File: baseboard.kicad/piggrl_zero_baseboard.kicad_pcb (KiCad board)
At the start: 2 copper layers, 101 x 43.9 mm, 62 parts, among them P1 PowerBoost 500c, P2 I2C, P3 USB_A, P4 Serial, Q1 IRF7309IPBF, Q3 Q_PMOS_GSD, Q4 MMBT2222, SW1 SW_PUSH, U1 gpio-header_zero, U2 2.2_tft_ili9340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

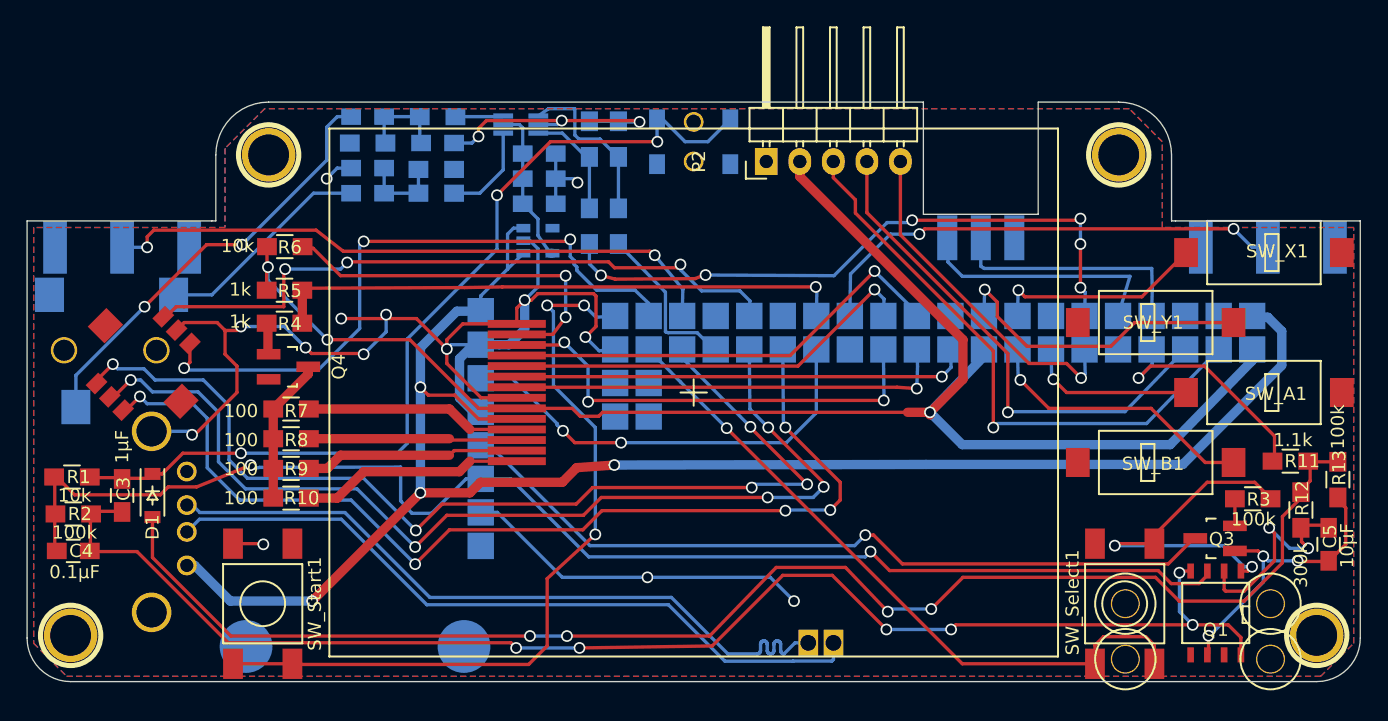
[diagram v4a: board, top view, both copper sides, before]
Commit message: ditch mosfet as softpower inverter and use same BJT transistor as the one used for the backlight
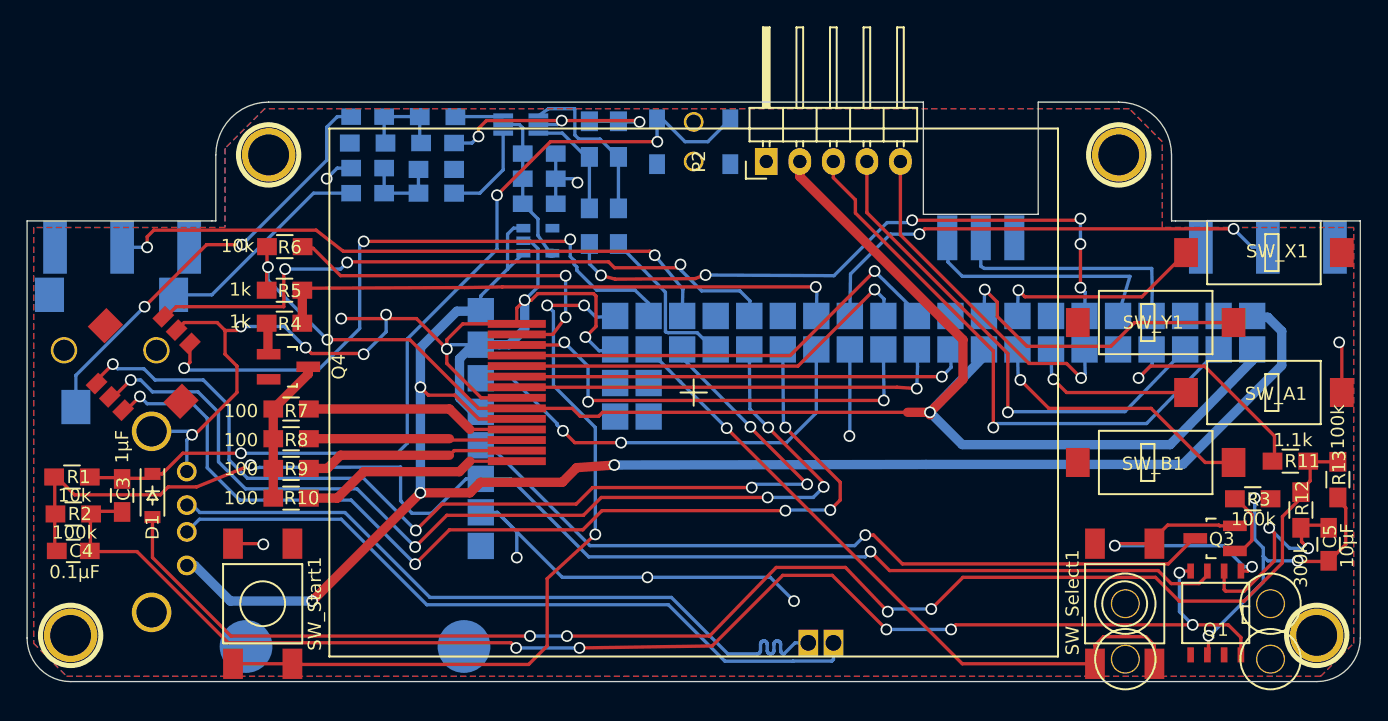
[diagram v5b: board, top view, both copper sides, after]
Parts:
- Q3: value Q_PMOS_GSD -> MMBT2222
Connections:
- Q3 pad 1: /soft_power_button/Vout -> Net-(Q3-Pad1)
- Q3 pad 2: Net-(Q3-Pad2) -> GND
- R3 pad 1: Net-(Q3-Pad2) -> Net-(Q3-Pad1)
- R3 pad 2: GND -> /soft_power_button/Vout
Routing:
- net GND: track 174.9 -> 187.4 mm, vias 19 -> 22
- net Net-(Q3-Pad1): track 0.00 -> 5.36 mm
- net /soft_power_button/Vout: track 22.2 -> 25.9 mm
- net Net-(Q3-Pad2): track 2.05 -> 0.00 mm

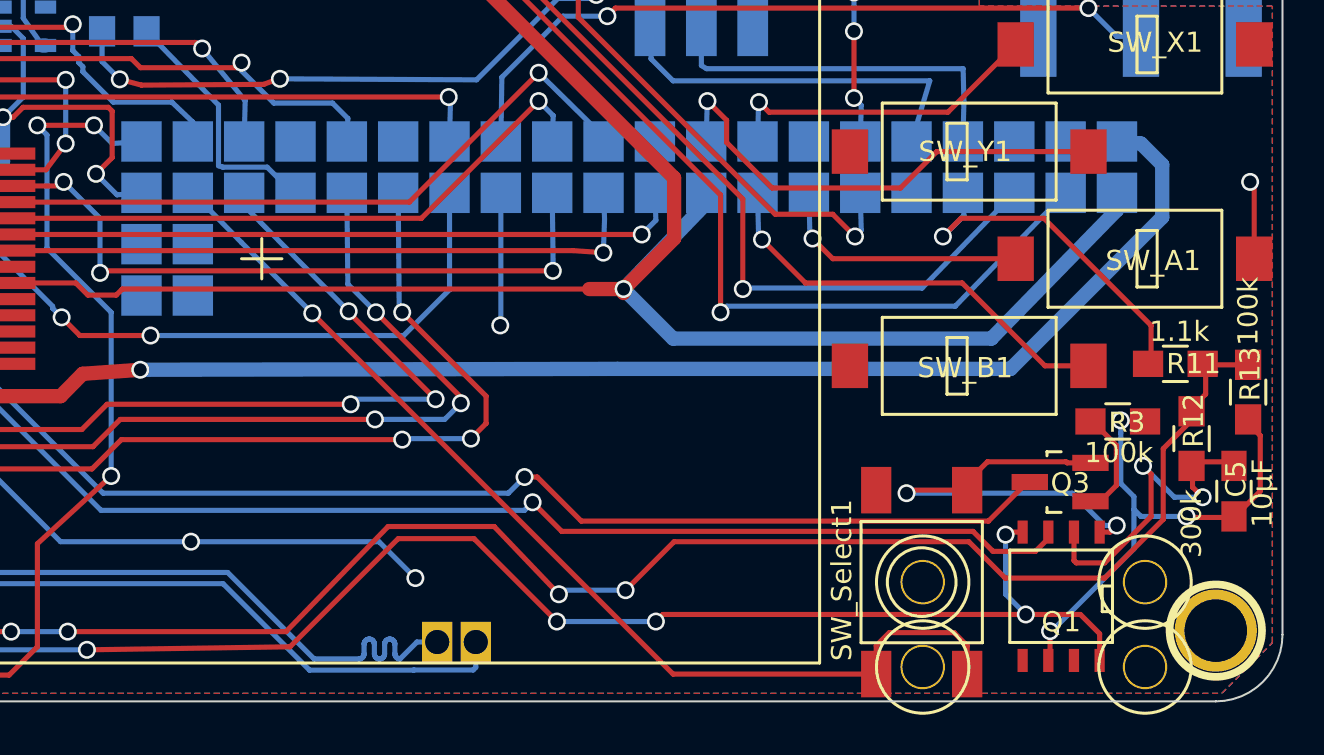
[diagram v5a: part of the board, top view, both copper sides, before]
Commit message: turns out we don't need the transistor (Q3) at all... so remove it, leaving only the 100k pulldown on the powerboosts enable pin
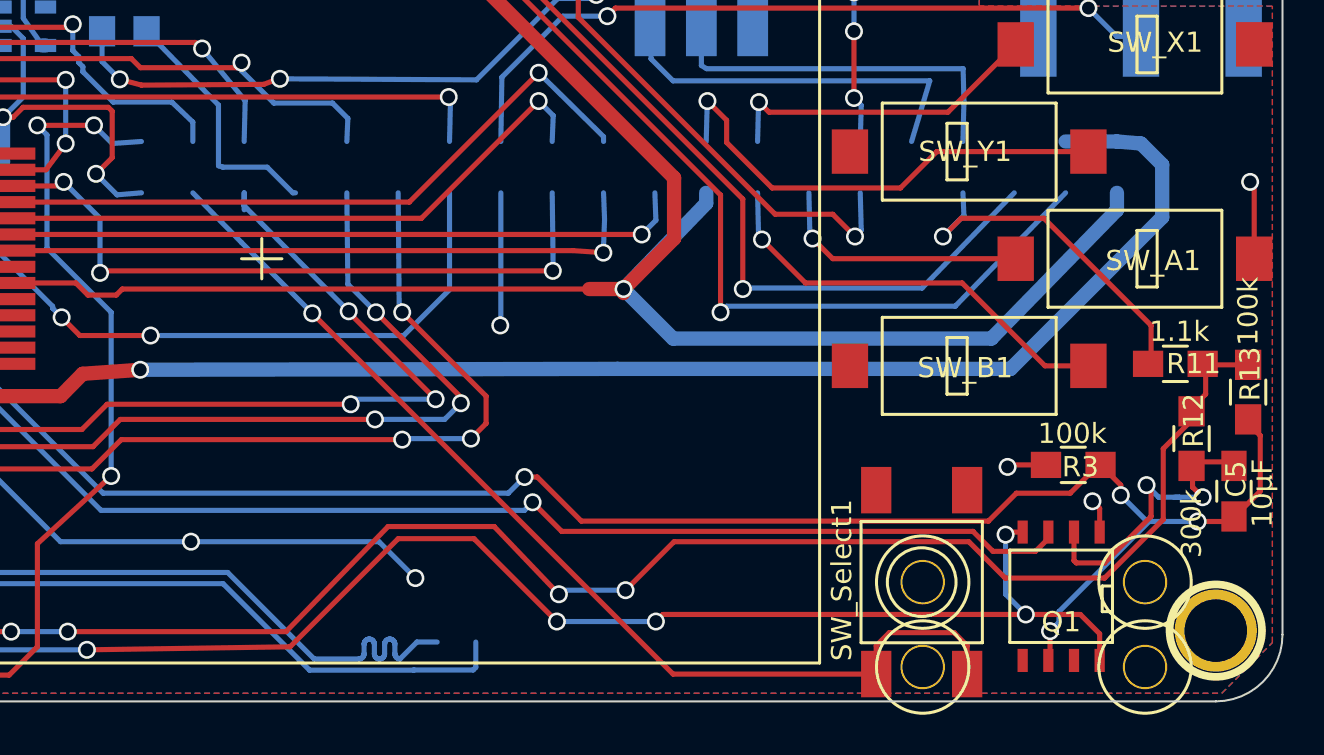
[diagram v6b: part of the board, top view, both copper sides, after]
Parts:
- removed Q3: MMBT2222, TO_SOT_Packages_SMD:SOT-23_Handsoldering
- removed U1: gpio-header_zero, components:raspberry-zero
- moved R3 3.08 mm to (207.7, 141.2), turned to 180 degrees
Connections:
- C5 pad 2: /soft_power_button/Vout -> Enable
- P1 pad 4: /Enable -> Enable
- Q1 pad 6: /soft_power_button/Vout -> Enable
- R13 pad 2: /soft_power_button/Vout -> Enable
- R3 pad 1: Net-(Q3-Pad1) -> Enable
- R3 pad 2: /soft_power_button/Vout -> GND
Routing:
- net Enable: track 0.00 -> 86.0 mm, vias 0 -> 4
- net /Enable: track 59.7 -> 0.00 mm, vias 1 -> 0
- net /soft_power_button/Vout: track 25.9 -> 0.00 mm, vias 3 -> 0
- net GND: track 187.4 -> 163.0 mm, vias 22 -> 21
- net (no net): track 0.00 -> 6.57 mm, vias 0 -> 1
- net Net-(Q3-Pad1): track 5.36 -> 0.00 mm
- net Net-(C5-Pad1): track 16.6 -> 15.3 mm

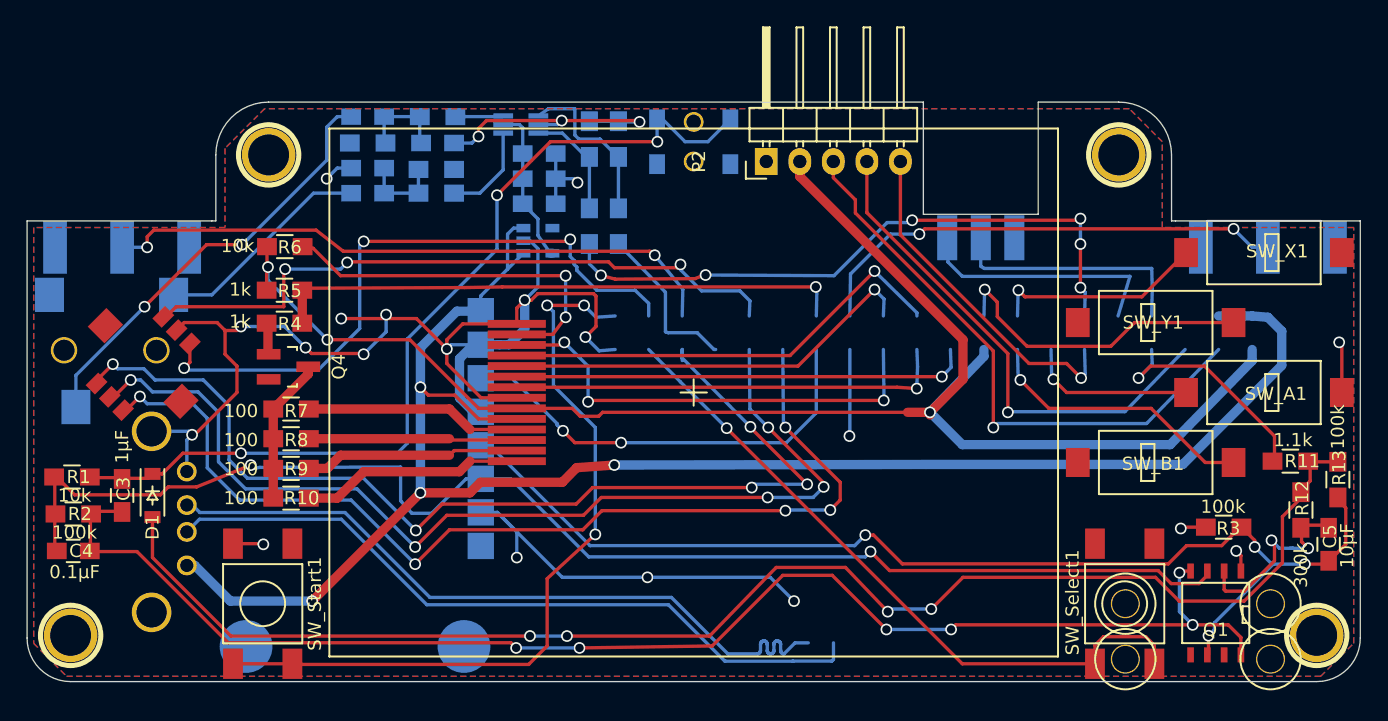
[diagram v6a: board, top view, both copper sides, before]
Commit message: cleanup some traces
and restore the accidentally deleted raspberry-footprint :-p
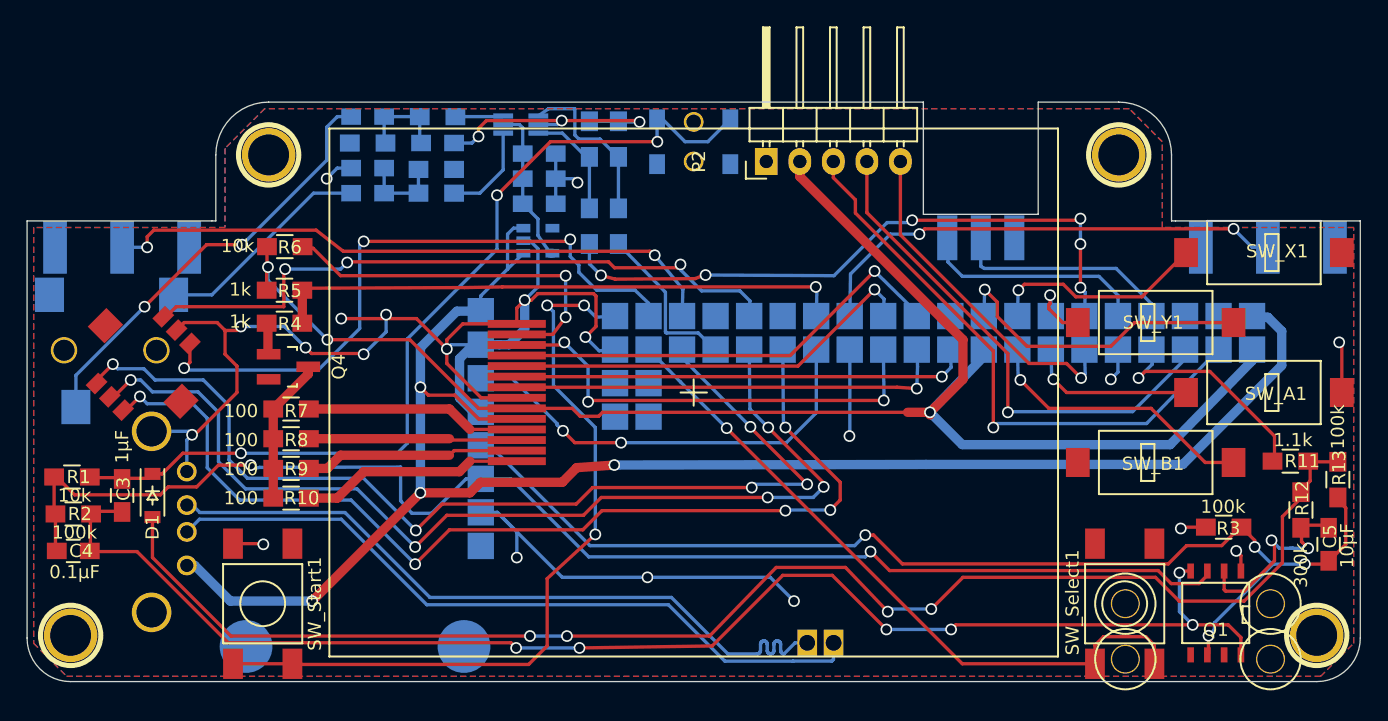
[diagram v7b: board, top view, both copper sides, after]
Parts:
- added U1: gpio-header_zero, components:raspberry-zero, B.Cu at (186.9, 137.9)
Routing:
- net GND: track 163.0 -> 177.4 mm, vias 21 -> 24
- net (no net): track 6.57 -> 0.00 mm, vias 1 -> 0
- net Net-(P4-Pad3): track 18.6 -> 16.7 mm
- net Net-(P4-Pad2): track 18.8 -> 17.2 mm

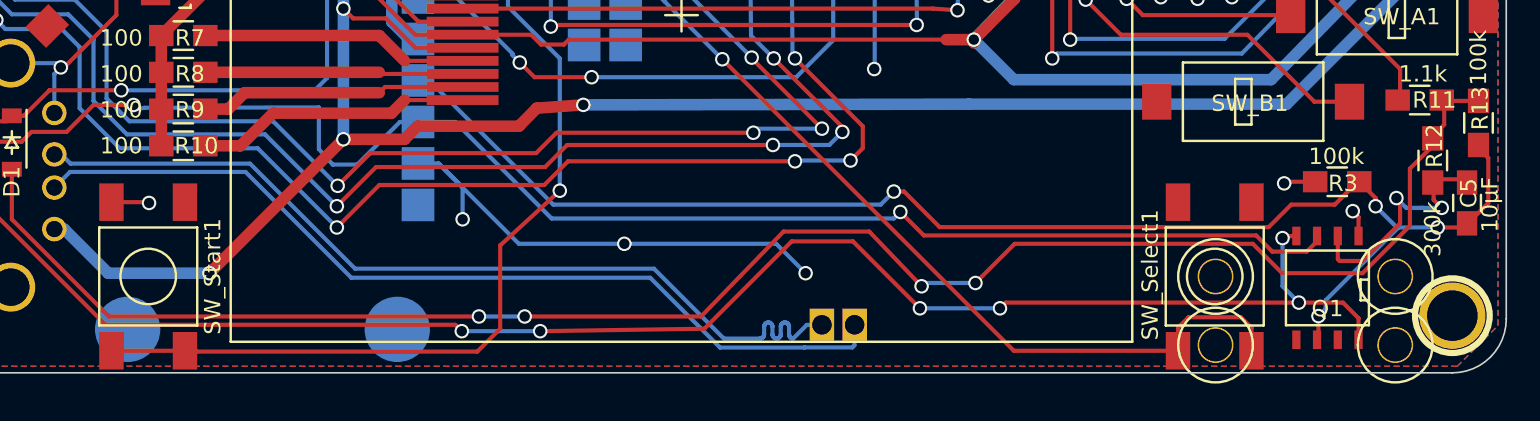
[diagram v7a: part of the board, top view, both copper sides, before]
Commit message: corrected usb-pad positions and mini-hdmi-tabs cutout based on 3d model
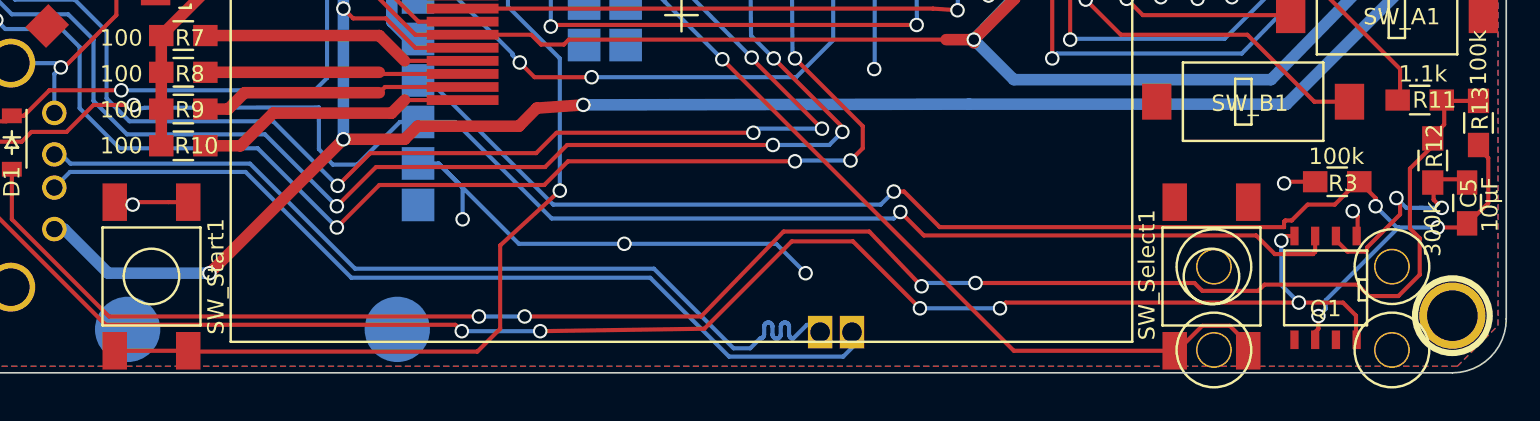
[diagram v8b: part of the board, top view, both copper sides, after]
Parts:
- moved REF** 0.63 mm to (211.0, 146.4)
- moved REF** 0.61 mm to (200.1, 146.4)
- moved REF** 0.36 mm to (211.0, 151.5)
- moved REF** 0.32 mm to (200.1, 151.5)
- moved SW_Select1 0.20 mm to (199.9, 147.0)
- moved SW_Start1 0.20 mm to (135.1, 147.0)
- moved Q1 0.12 mm to (206.9, 147.7)
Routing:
- net GND: track 177.4 -> 179.8 mm
- net Net-(D1-Pad2): track 108.7 -> 110.8 mm
- net Net-(C5-Pad1): track 15.3 -> 14.0 mm
- net /btn_8: track 50.9 -> 49.6 mm
